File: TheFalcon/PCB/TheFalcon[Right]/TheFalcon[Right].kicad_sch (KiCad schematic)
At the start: 45 parts, among them J1 Conn_01x01, J2 Conn_01x04_Pin, J3 Conn_01x01, J4 Conn_01x01, J5 Conn_01x01, J7 Conn_01x01, SW1 SW_Push, SW2 SW_Push, U2 USBLC6-2P6, U3 USBLC6-2P6, U4 AMS1117-3.3, U6 STM32G431CBTx, Y1 X322516MOB4SI

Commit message: Save
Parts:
- removed R1, R2: 5.1k, Resistor_SMD:R_0603_1608Metric, symbol Device:R
- removed U2: USBLC6-2P6, Package_TO_SOT_SMD:SOT-666, symbol Power_Protection:USBLC6-2P6
- removed USB1: USB_C_Receptacle_USB2.0_16P, Connector_USB:USB_C_Receptacle_G-Switch_GT-USB-7010ASV, symbol Connector:USB_C_Receptacle_USB2.0_16P
- renumbered C2 to C12, C9 to C13, C3 to C14, C1 to C9, D1 to D39, J3 to J2, J4 to J3, J7 to J4, J2 to J5, J5 to J6, J1 to J7, R1 to R3, R33 to R4, R2 to R5, R3 to R6, R4 to R7, SW2 to SW1, SW1 to SW2, U6 to U1
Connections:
- net USB_MCU_D- is gone; now on net Col0: U1.33 (PA11)
- net Col0: no longer U1.32 (PA10)
- net Col1: now also U1.32 (PA10); no longer U1.29 (PB15)
- net LED_MCU_SDB: now also U1.15 (PA7); no longer U1.9 (PA1)
- net Row4: now also U1.2 (PC13); no longer U1.14 (PA6)
- net ThumbRow: now also U1.14 (PA6); no longer U1.2 (PC13)
- net USB_MCU_D+: no longer names the net of U1.34 (PA12)
- no-connect marks 17 -> 16
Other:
- note added: "ESD Protection for the USB interface"
- note removed: "ESD Protection for the two USB interfaces"
- note removed: "USB to PC Connector"
- moved on the sheet: R3, R4

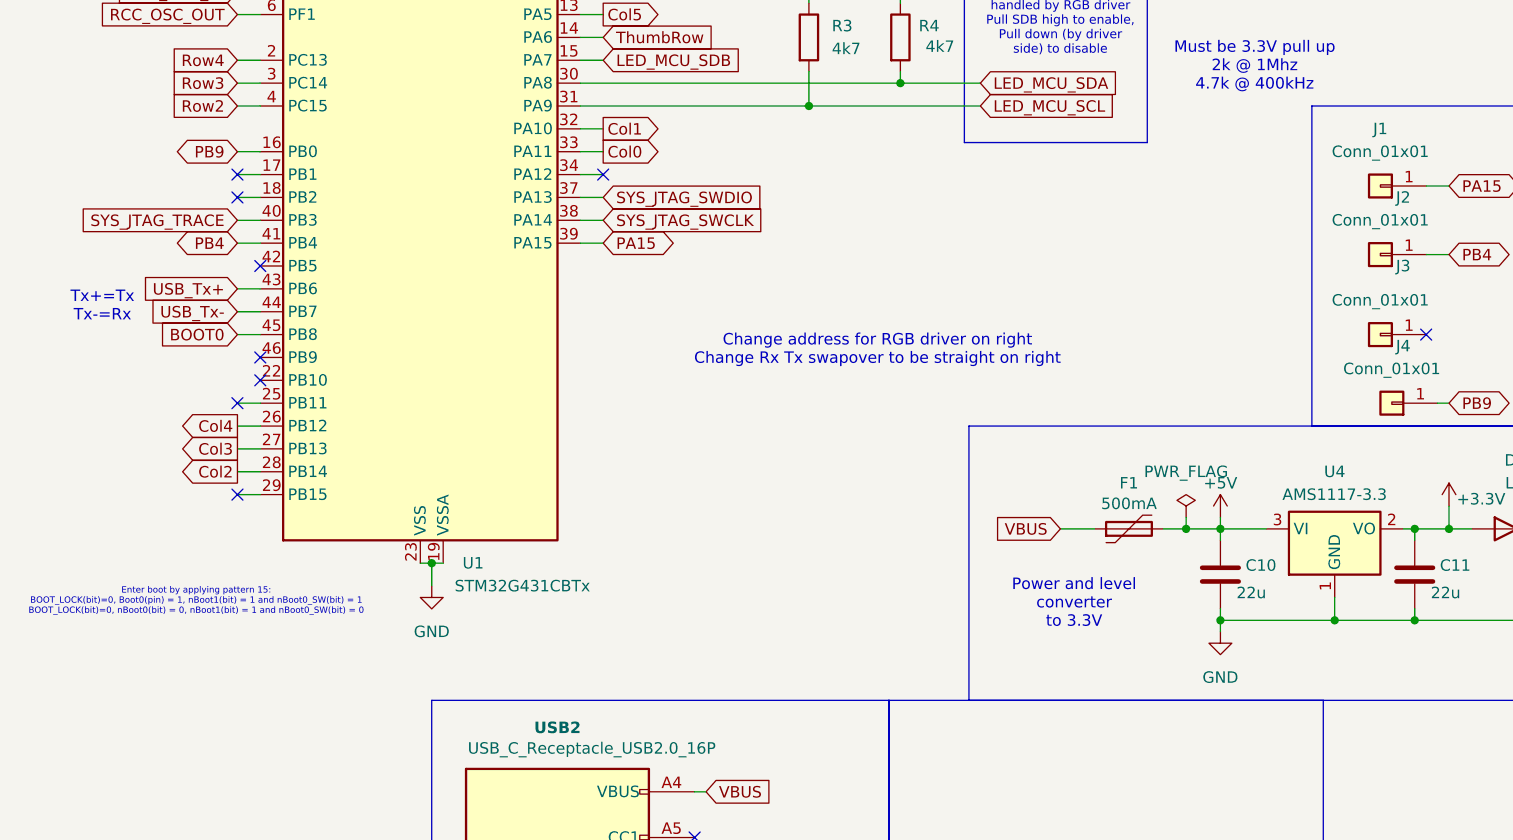
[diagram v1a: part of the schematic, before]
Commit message: Right Side Done
Need to check but right side looks good
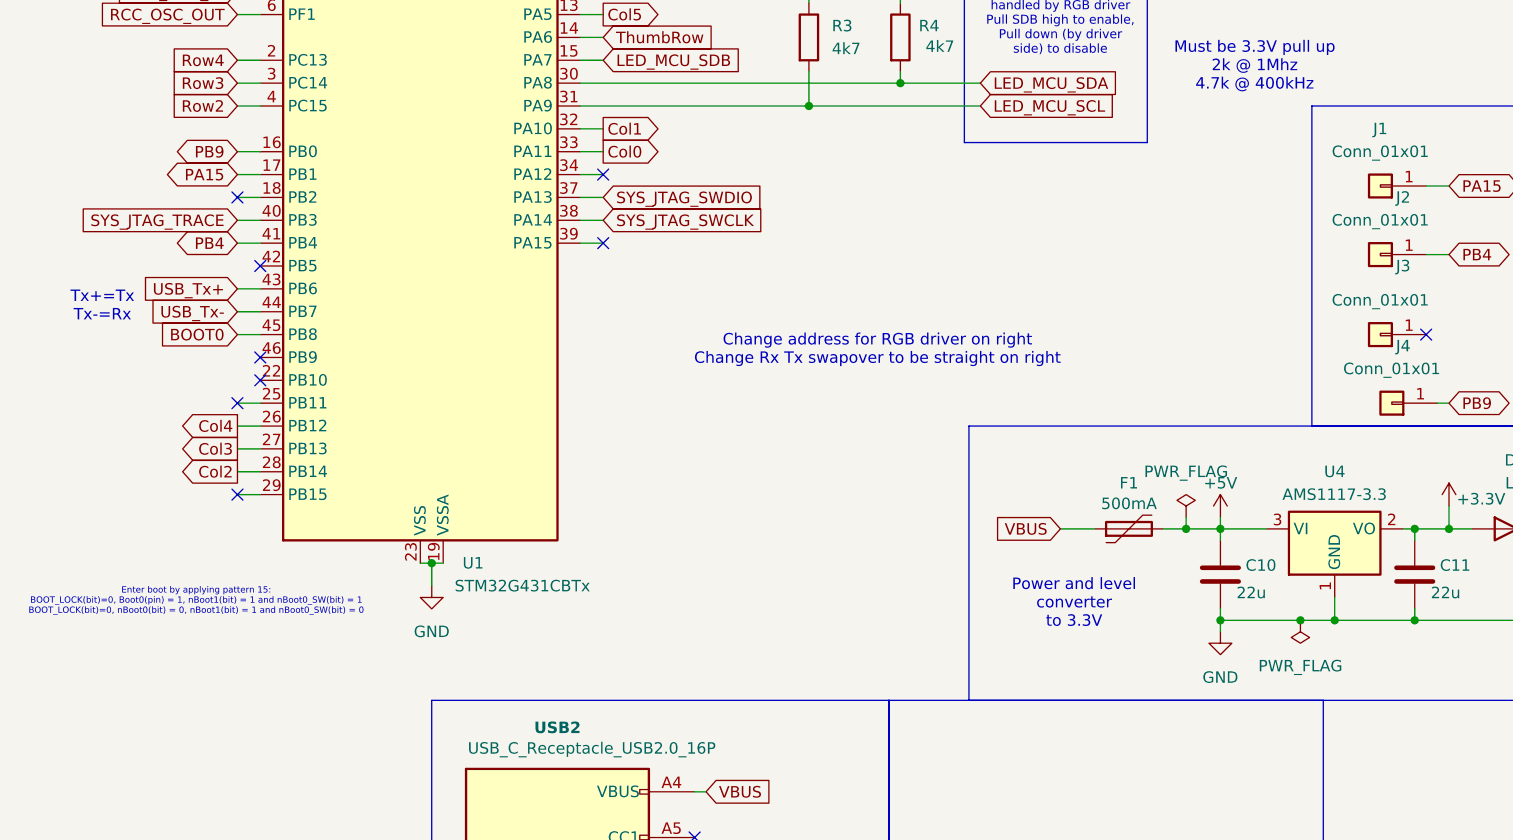
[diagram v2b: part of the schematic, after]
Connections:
- net PA15: now also U1.17 (PB1); no longer U1.39 (PA15)
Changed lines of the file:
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@@
 	)
 	(junction
+		(at 163.83 128.27)
+		(diameter 0)
+		(color 0 0 0 0)
+	)
+	(junction
 		(at 49.53 35.56)
 		(diameter 0)
@@
 	)
 	(no_connect
-		(at 45.72 78.74)
+		(at 86.36 86.36)
 	)
 	(no_connect
@@
 	(wire
 		(pts
+			(xy 163.83 128.27) (xy 167.64 128.27)
+		)
+		(stroke
+			(width 0)
+			(type default)
+		)
+	)
+	(wire
+		(pts
 			(xy 149.86 48.26) (xy 147.32 48.26)
 		)
@@
 	(wire
 		(pts
-			(xy 154.94 128.27) (xy 167.64 128.27)
+			(xy 154.94 128.27) (xy 163.83 128.27)
 		)
 		(stroke
@@
 	(global_label "PA15"
 		(shape bidirectional)
-		(at 86.36 86.36 0)
+		(at 45.72 78.74 180)
 		(fields_autoplaced yes)
 		(effects
@@
 				(size 1.27 1.27)
 			)
-			(justify left)
+			(justify right)
 		)
 		(property "Intersheetrefs" "${INTERSHEET_REFS}"
-			(at 95.2341 86.36 0)
+			(at 36.8459 78.74 0)
 			(effects
 				(font
 					(size 1.27 1.27)
 				)
-				(justify left)
+				(justify right)
 				(hide yes)
 			)
@@
 		)
 	)
-	(global_label "PA15"
+	(global_label "PB9"
 		(shape bidirectional)
-		(at 180.34 80.01 0)
+		(at 180.34 104.14 0)
 		(fields_autoplaced yes)
 		(effects
@@
 		)
 		(property "Intersheetrefs" "${INTERSHEET_REFS}"
-			(at 189.2141 80.01 0)
+			(at 188.186 104.14 0)
 			(effects
 				(font
@@
 		)
 	)
-	(global_label "PB9"
-		(shape bidirectional)
-		(at 180.34 104.14 0)
+	(global_label "SYS_JTAG_SWDIO"
+		(shape input)
+		(at 233.68 67.31 0)
 		(fields_autoplaced yes)
 		(effects
@@
 		)
 		(property "Intersheetrefs" "${INTERSHEET_REFS}"
-			(at 188.186 104.14 0)
+			(at 252.268 67.31 0)
 			(effects
 				(font
@@
 	(global_label "SYS_JTAG_SWDIO"
 		(shape input)
-		(at 233.68 67.31 0)
+		(at 86.36 81.28 0)
 		(fields_autoplaced yes)
 		(effects
@@
 		)
 		(property "Intersheetrefs" "${INTERSHEET_REFS}"
-			(at 252.268 67.31 0)
+			(at 104.948 81.28 0)
 			(effects
 				(font
@@
 		)
 	)
-	(global_label "SYS_JTAG_SWDIO"
+	(global_label "USB_CONN_Tx+"
 		(shape input)
-		(at 86.36 81.28 0)
+		(at 99.06 166.37 0)
 		(fields_autoplaced yes)
 		(effects
@@
 		)
 		(property "Intersheetrefs" "${INTERSHEET_REFS}"
-			(at 104.948 81.28 0)
+			(at 116.62 166.37 0)
 			(effects
 				(font
@@
 		)
 	)
-	(global_label "USB_CONN_Tx+"
-		(shape input)
-		(at 99.06 166.37 0)
+	(global_label "Col1"
+		(shape output)
+		(at 86.36 73.66 0)
 		(fields_autoplaced yes)
 		(effects
@@
 		)
 		(property "Intersheetrefs" "${INTERSHEET_REFS}"
-			(at 116.62 166.37 0)
+			(at 93.6389 73.66 0)
 			(effects
 				(font
@@
 		)
 	)
-	(global_label "Col1"
-		(shape output)
-		(at 86.36 73.66 0)
+	(global_label "PA15"
+		(shape bidirectional)
+		(at 180.34 80.01 0)
 		(fields_autoplaced yes)
 		(effects
@@
 		)
 		(property "Intersheetrefs" "${INTERSHEET_REFS}"
-			(at 93.6389 73.66 0)
+			(at 189.2141 80.01 0)
 			(effects
 				(font
@@
 					(unit 1)
 				)
+			)
+		)
+	)
+	(symbol
+		(lib_id "power:PWR_FLAG")
+		(at 163.83 128.27 180)
+		(unit 1)
+		(exclude_from_sim no)
+		(in_bom yes)
+		(on_board yes)
+		(dnp no)
+		(fields_autoplaced yes)
+		(property "Reference" "#FLG01"
+			(at 163.83 130.175 0)
+			(effects
+				(font
+					(size 1.27 1.27)
+				)
+				(hide yes)
+			)
+		)
+		(property "Value" "PWR_FLAG"
+			(at 163.83 133.35 0)
+			(effects
+				(font
+					(size 1.27 1.27)
+				)
+			)
+		)
+		(property "Footprint" ""
+			(at 163.83 128.27 0)
+			(effects
+				(font
+					(size 1.27 1.27)
+				)
+				(hide yes)
+			)
+		)
+		(property "Datasheet" "~"
+			(at 163.83 128.27 0)
+			(effects
+				(font
+					(size 1.27 1.27)
+				)
+				(hide yes)
+			)
+		)
+		(property "Description" "Special symbol for telling ERC where power comes from"
+			(at 163.83 128.27 0)
+			(effects
+				(font
+					(size 1.27 1.27)
+				)
+				(hide yes)
+			)
+		)
+		(pin "1"
+		)
+		(instances
+			(project "TheFalcon[Right]"
+				(path "/c04da171-1d33-4593-80a3-c384d6d19f7c"
+					(reference "#FLG01")
+					(unit 1)
+				)

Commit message: Save
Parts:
- removed H1, H2, H3, H4, H5, H6: MountingHole_Pad, MountingHole:MountingHole_2.2mm_M2_Pad, symbol Mechanical:MountingHole_Pad

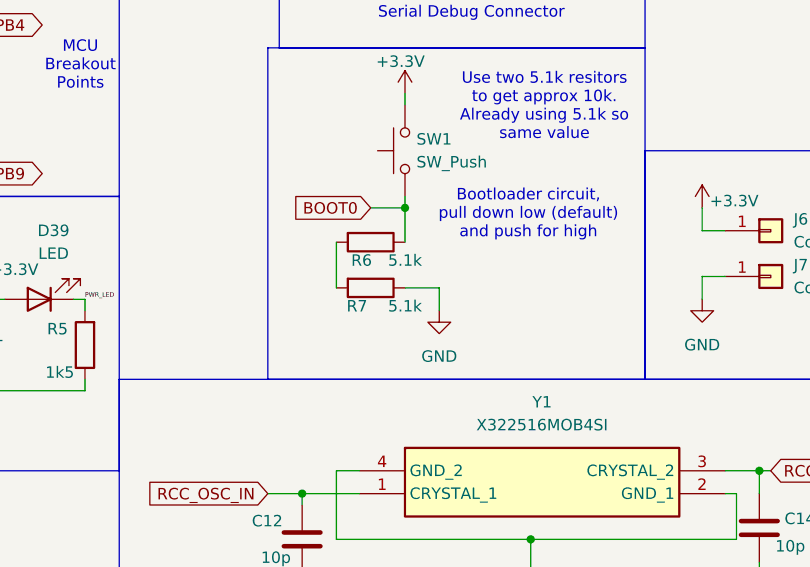
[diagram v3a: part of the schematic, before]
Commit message: Files ready for production
Going to panelise seperate files to reduce PCBA cost
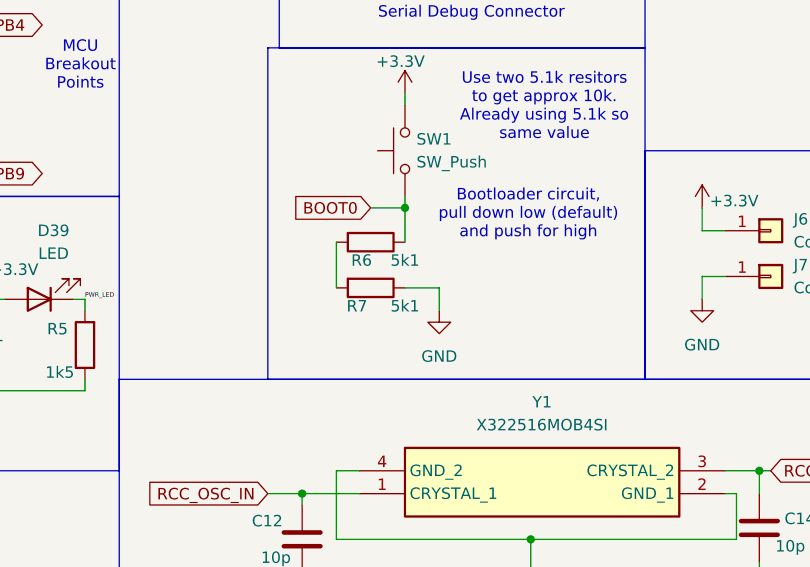
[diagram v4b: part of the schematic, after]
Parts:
- C1: LCSC Part Number (none) -> C1713
- C10, C11: LCSC Part Number (none) -> C1859
- C12, C14: LCSC Part Number (none) -> C1545
- C13, C2, C3, C4, C5, C8: LCSC Part Number (none) -> C1525
- C6: LCSC Part Number (none) -> C1524
- C7, C9: LCSC Part Number (none) -> C1592
- D39: LCSC Part Number (none) -> C84260
- F1: LCSC Part Number (none) -> C135336
- R3, R4: LCSC Part Number (none) -> C23162
- R5: LCSC Part Number (none) -> C22843
- R6, R7: value 5.1k -> 5k1; LCSC Part Number (none) -> C23067
- SW1, SW2: footprint Button_Switch_SMD:SW_SPST_B3U-1000P -> CustomSPDTButton:SPDT_Switch_KiCad_BasicComponent; LCSC Part Number (none) -> C231329
- U1: LCSC Part Number (none) -> C529355
- U3: LCSC Part Number (none) -> C29780639
- U4: LCSC Part Number (none) -> C6186; Link https://jlcpcb.com/partdetail/Advanced_MonolithicSystems-AM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 -> (none)
- USB2: LCSC Part Number (none) -> C2988369; Link https://jlcpcb.com/partdetail/gswitch-GT_USB7010ASV/C2988369 -> (none)
- Y1: Height 0.8 -> (none); LCSC Part Number (none) -> C12668; Link1 https://jlcpcb.com/partdetail/Yxc_CrystalOscillators-X32251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 -> (none); Link2 https://za.rs-online.com/web/p/crystal-units/1712765?cm_mmc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 -> (none); Manufacturer_Name Yangxing Tech -> (none); Manufacturer_Part_Number X322516MOB4SI -> (none)
